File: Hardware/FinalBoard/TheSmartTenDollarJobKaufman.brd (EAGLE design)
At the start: 55 x 55.4 mm, 50 parts, among them IC1 74HC595D, IC2 74HC595D, IC3 74HC595D, IC4 74HC595D

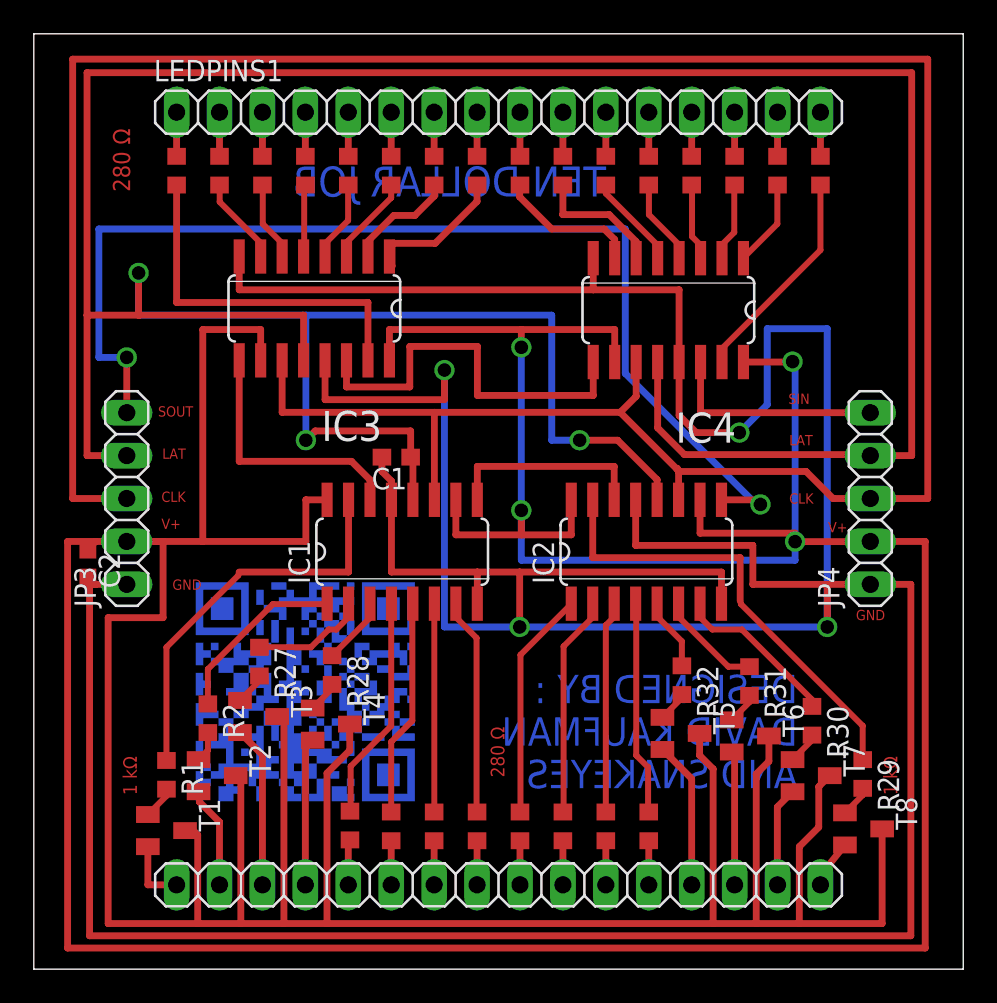
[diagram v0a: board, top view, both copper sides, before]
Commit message: Updated board, added pecker logo.
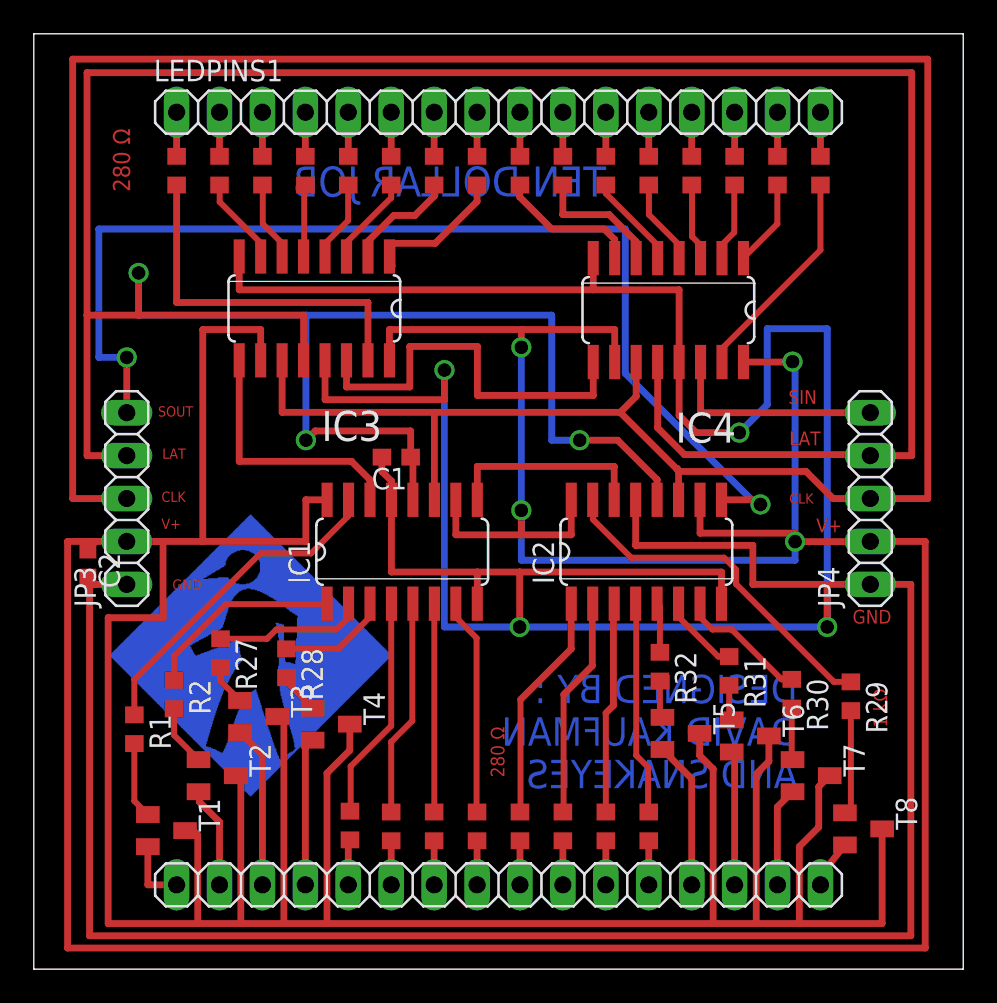
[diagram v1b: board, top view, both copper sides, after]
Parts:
- moved R29 4.65 mm to (48.4, 15.8)
- moved R1 3.30 mm to (5.95, 13.8)
- moved R28 2.73 mm to (14.9, 17.8)
- moved R2 2.44 mm to (8.30, 15.9)
- moved R27 2.35 mm to (11.1, 18.4)
- moved R30 2.00 mm to (44.9, 15.9)
- moved R32 1.53 mm to (37.0, 17.6)
- moved R31 1.34 mm to (41.1, 17.3)
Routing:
- net QH: track 27.1 -> 20.9 mm
- net N$61: track 1.88 -> 6.19 mm
- net QA: track 23.7 -> 19.7 mm
- net N$34: track 1.96 -> 4.53 mm
- net QD: track 4.01 -> 6.52 mm
- net QG: track 9.85 -> 7.75 mm
- net QC: track 6.81 -> 8.90 mm
- net N$58: track 1.83 -> 3.60 mm
- net QF: track 6.20 -> 4.75 mm
- net QE: track 4.28 -> 2.94 mm
- net N$62: track 1.93 -> 3.07 mm
- net QB: track 10.7 -> 11.8 mm
- net N$60: track 1.88 -> 2.44 mm
